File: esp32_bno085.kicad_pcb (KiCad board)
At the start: 2 copper layers, 24.5 x 53.4 mm, 36 parts, among them J1 530480210, J2 USB_C_Receptacle_USB2.0_16P, Q1 AO3401A, SW1 RESET, SW2 BOOT, U1 TP4056-42-ESOP8, U2 ESP32-S3-WROOM-1, U3 BNO085, U4 XC6220B331MR, Y1 32.7680kHz

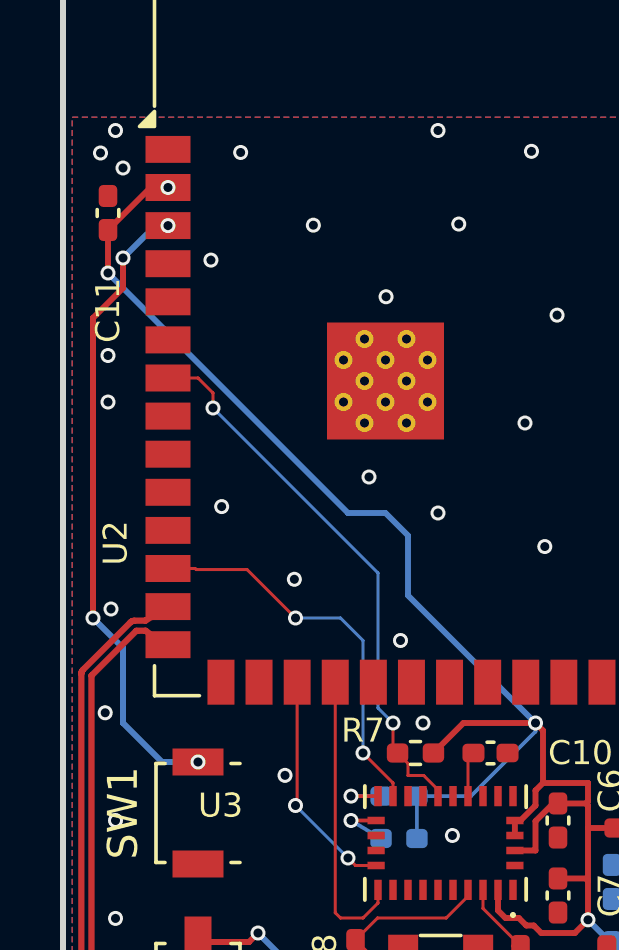
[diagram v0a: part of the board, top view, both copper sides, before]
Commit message: Improve JLCPCB assembly via handling
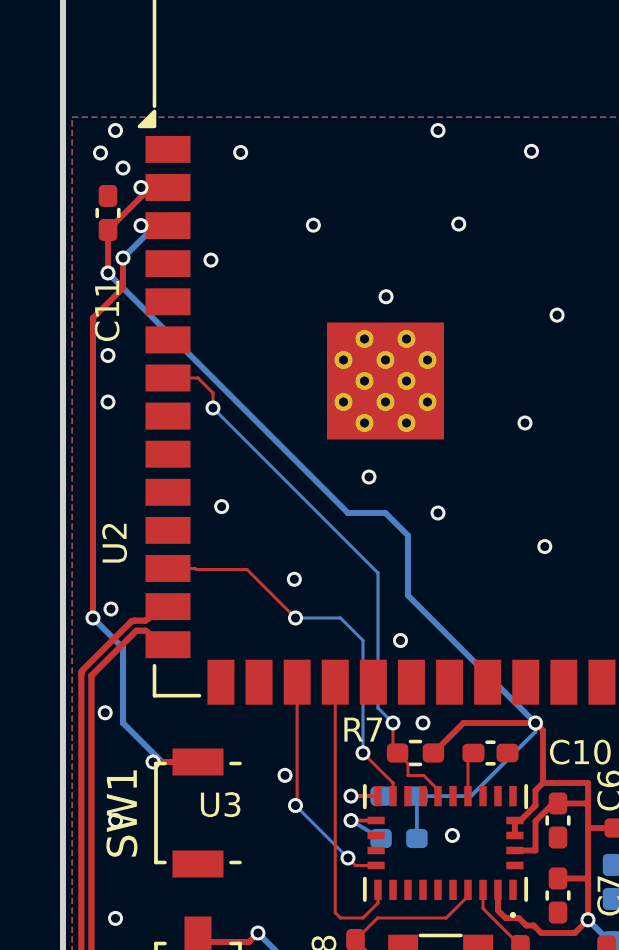
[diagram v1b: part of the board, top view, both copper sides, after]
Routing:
- net ESP_EN: track 21.4 -> 23.3 mm
- net +3.3V: track 59.8 -> 60.4 mm

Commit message: Clarify VSYS rail and JLCPCB order notes
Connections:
- net Net-(D1-K) renamed VSYS
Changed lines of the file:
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@@
 			(layers "F.Cu" "F.Mask" "F.Paste")
 			(roundrect_rratio 0.25)
-			(net "Net-(D1-K)")
+			(net "VSYS")
 			(pinfunction "K")
 			(pintype "passive")
@@
 			(layers "F.Cu" "F.Mask" "F.Paste")
 			(roundrect_rratio 0.25)
-			(net "Net-(D1-K)")
+			(net "VSYS")
 			(pinfunction "D")
 			(pintype "passive")
@@
 			(layers "B.Cu" "B.Mask" "B.Paste")
 			(roundrect_rratio 0.25)
-			(net "Net-(D1-K)")
+			(net "VSYS")
 			(pinfunction "VIN")
 			(pintype "power_in")
@@
 			(layers "B.Cu" "B.Mask" "B.Paste")
 			(roundrect_rratio 0.25)
-			(net "Net-(D1-K)")
+			(net "VSYS")
 			(pinfunction "CE")
 			(pintype "input")
@@
 			(layers "B.Cu" "B.Mask" "B.Paste")
 			(roundrect_rratio 0.25)
-			(net "Net-(D1-K)")
+			(net "VSYS")
 			(pintype "passive")
 		)
@@
 		(width 0.101702)
 		(layer "F.Cu")
-		(net "Net-(D1-K)")
+		(net "VSYS")
 	)
 	(segment
@@
 		(width 0.101702)
 		(layer "F.Cu")
-		(net "Net-(D1-K)")
+		(net "VSYS")
 	)
 	(segment
@@
 		(width 0.101702)
 		(layer "F.Cu")
-		(net "Net-(D1-K)")
+		(net "VSYS")
 	)
 	(segment
@@
 		(width 0.101702)
 		(layer "F.Cu")
-		(net "Net-(D1-K)")
+		(net "VSYS")
 	)
 	(segment
@@
 		(width 0.101702)
 		(layer "F.Cu")
-		(net "Net-(D1-K)")
+		(net "VSYS")
 	)
 	(segment
@@
 		(width 0.101702)
 		(layer "F.Cu")
-		(net "Net-(D1-K)")
+		(net "VSYS")
 	)
 	(segment
@@
 		(width 0.101702)
 		(layer "F.Cu")
-		(net "Net-(D1-K)")
+		(net "VSYS")
 	)
 	(via
@@
 		)
 		(filling no)
-		(net "Net-(D1-K)")
+		(net "VSYS")
 	)
 	(via
@@
 		)
 		(filling no)
-		(net "Net-(D1-K)")
+		(net "VSYS")
 	)
 	(segment
@@
 		(width 0.101702)
 		(layer "B.Cu")
-		(net "Net-(D1-K)")
+		(net "VSYS")
 	)
 	(segment
@@
 		(width 0.101702)
 		(layer "B.Cu")
-		(net "Net-(D1-K)")
+		(net "VSYS")
 	)
 	(segment
@@
 		(width 0.101702)
 		(layer "B.Cu")
-		(net "Net-(D1-K)")
+		(net "VSYS")
 	)
 	(segment
@@
 		(width 0.101702)
 		(layer "B.Cu")
-		(net "Net-(D1-K)")
+		(net "VSYS")
 	)
 	(segment
@@
 		(width 0.101702)
 		(layer "B.Cu")
-		(net "Net-(D1-K)")
+		(net "VSYS")
 	)
 	(segment
@@
 		(width 0.101702)
 		(layer "B.Cu")
-		(net "Net-(D1-K)")
+		(net "VSYS")
 	)
 	(segment
@@
 		(width 0.101702)
 		(layer "B.Cu")
-		(net "Net-(D1-K)")
+		(net "VSYS")
 	)
 	(segment
@@
 		(width 0.101702)
 		(layer "B.Cu")
-		(net "Net-(D1-K)")
+		(net "VSYS")
 	)
 	(segment
@@
 		(width 0.101702)
 		(layer "B.Cu")
-		(net "Net-(D1-K)")
+		(net "VSYS")
 	)
 	(segment
@@
 		(width 0.101702)
 		(layer "B.Cu")
-		(net "Net-(D1-K)")
+		(net "VSYS")
 	)
 	(segment
@@
 		(width 0.101702)
 		(layer "B.Cu")
-		(net "Net-(D1-K)")
+		(net "VSYS")
 	)
 	(segment
@@
 		(width 0.101702)
 		(layer "B.Cu")
-		(net "Net-(D1-K)")
+		(net "VSYS")
 	)
 	(segment
@@
 		(width 0.101702)
 		(layer "B.Cu")
-		(net "Net-(D1-K)")
+		(net "VSYS")
 	)
 	(segment
@@
 		(width 0.101702)
 		(layer "B.Cu")
-		(net "Net-(D1-K)")
+		(net "VSYS")
 	)
 	(segment
@@
 		(width 0.101702)
 		(layer "B.Cu")
-		(net "Net-(D1-K)")
+		(net "VSYS")
 	)
 	(segment
@@
 		(width 0.101702)
 		(layer "B.Cu")
-		(net "Net-(D1-K)")
+		(net "VSYS")
 	)
 	(zone

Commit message: Clarify stock scope and add PCB fiducials
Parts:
- added FID1: Fiducial_1mm_Mask2mm, Fiducial:Fiducial_1mm_Mask2mm, F.Cu at (102.5, 88.0)
- added FID2: Fiducial_1mm_Mask2mm, Fiducial:Fiducial_1mm_Mask2mm, F.Cu at (120.0, 88.0)
- added FID3: Fiducial_1mm_Mask2mm, Fiducial:Fiducial_1mm_Mask2mm, F.Cu at (120.0, 91.0)
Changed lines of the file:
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@@
 			)
 		)
-		(property "BOM Comments" "LCSC page showed this part out of stock on 2026-07-13; verify JLCPCB pre-order/availability before PCBA."
+		(property "BOM Comments" "Lab inventory available per user; stock verification intentionally skipped. If using JLC-sourced turnkey PCBA, re-check C5189642 availability."
 			(at 0 0 180)
 			(unlocked yes)
@@
 		)
 	)
+	(footprint "Fiducial:Fiducial_1mm_Mask2mm"
+		(layer "F.Cu")
+		(at 102.5 88)
+		(descr "Fiducial, circular marking, 1mm bare copper, 2mm soldermask opening")
+		(tags "fiducial")
+		(property "Reference" "FID1"
+			(at 0 -1.95 0)
+			(layer "F.SilkS")
+			(hide yes)
+			(effects
+				(font
+					(size 1 1)
+					(thickness 0.15)
+				)
+			)
+		)
+		(property "Value" "Fiducial_1mm_Mask2mm"
+			(at 0 1.95 0)
+			(layer "F.Fab")
+			(hide yes)
+			(effects
+				(font
+					(size 1 1)
+					(thickness 0.15)
+				)
+			)
+		)
+		(attr smd board_only exclude_from_pos_files exclude_from_bom)
+		(duplicate_pad_numbers_are_jumpers no)
+		(fp_circle
+			(center 0 0)
+			(end 1.25 0)
+			(stroke
+				(width 0.05)
+				(type solid)
+			)
+			(fill no)
+			(layer "F.CrtYd")
+		)
+		(fp_circle
+			(center 0 0)
+			(end 1 0)
+			(stroke
+				(width 0.1)
+				(type solid)
+			)
+			(fill no)
+			(layer "F.Fab")
+		)
+		(pad "" smd circle
+			(at 0 0)
+			(size 1 1)
+			(layers "F.Cu" "F.Mask")
+			(solder_mask_margin 0.5)
+			(clearance 0.6)
+		)
+		(embedded_fonts no)
+	)
+	(footprint "Fiducial:Fiducial_1mm_Mask2mm"
+		(layer "F.Cu")
+		(at 120 88)
+		(descr "Fiducial, circular marking, 1mm bare copper, 2mm soldermask opening")
+		(tags "fiducial")
+		(property "Reference" "FID2"
+			(at 0 -1.95 0)
+			(layer "F.SilkS")
+			(hide yes)
+			(effects
+				(font
+					(size 1 1)
+					(thickness 0.15)
+				)
+			)
+		)
+		(property "Value" "Fiducial_1mm_Mask2mm"
+			(at 0 1.95 0)
+			(layer "F.Fab")
+			(hide yes)
+			(effects
+				(font
+					(size 1 1)
+					(thickness 0.15)
+				)
+			)
+		)
+		(attr smd board_only exclude_from_pos_files exclude_from_bom)
+		(duplicate_pad_numbers_are_jumpers no)
+		(fp_circle
+			(center 0 0)
+			(end 1.25 0)
+			(stroke
+				(width 0.05)
+				(type solid)
+			)
+			(fill no)
+			(layer "F.CrtYd")
+		)
+		(fp_circle
+			(center 0 0)
+			(end 1 0)
+			(stroke
+				(width 0.1)
+				(type solid)
+			)
+			(fill no)
+			(layer "F.Fab")
+		)
+		(pad "" smd circle
+			(at 0 0)
+			(size 1 1)
+			(layers "F.Cu" "F.Mask")
+			(solder_mask_margin 0.5)
+			(clearance 0.6)
+		)
+		(embedded_fonts no)
+	)
+	(footprint "Fiducial:Fiducial_1mm_Mask2mm"
+		(layer "F.Cu")
+		(at 120 91)
+		(descr "Fiducial, circular marking, 1mm bare copper, 2mm soldermask opening")
+		(tags "fiducial")
+		(property "Reference" "FID3"
+			(at 0 -1.95 0)
+			(layer "F.SilkS")
+			(hide yes)
+			(effects
+				(font
+					(size 1 1)
+					(thickness 0.15)
+				)
+			)
+		)
+		(property "Value" "Fiducial_1mm_Mask2mm"
+			(at 0 1.95 0)
+			(layer "F.Fab")
+			(hide yes)
+			(effects
+				(font
+					(size 1 1)
+					(thickness 0.15)
+				)
+			)
+		)
+		(attr smd board_only exclude_from_pos_files exclude_from_bom)
+		(duplicate_pad_numbers_are_jumpers no)
+		(fp_circle
+			(center 0 0)
+			(end 1.25 0)
+			(stroke
+				(width 0.05)
+				(type solid)
+			)
+			(fill no)
+			(layer "F.CrtYd")
+		)
+		(fp_circle
+			(center 0 0)
+			(end 1 0)
+			(stroke
+				(width 0.1)
+				(type solid)
+			)
+			(fill no)
+			(layer "F.Fab")
+		)
+		(pad "" smd circle
+			(at 0 0)
+			(size 1 1)
+			(layers "F.Cu" "F.Mask")
+			(solder_mask_margin 0.5)
+			(clearance 0.6)
+		)
+		(embedded_fonts no)
+	)
 	(gr_rect

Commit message: Normalize capacitor BOM value and refresh JLC notes
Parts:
- C5: value 0.1uf -> 0.1uF
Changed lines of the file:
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@@
 			)
 		)
-		(property "Value" "0.1uf"
+		(property "Value" "0.1uF"
 			(at -0.25 0.75 0)
 			(layer "F.SilkS")

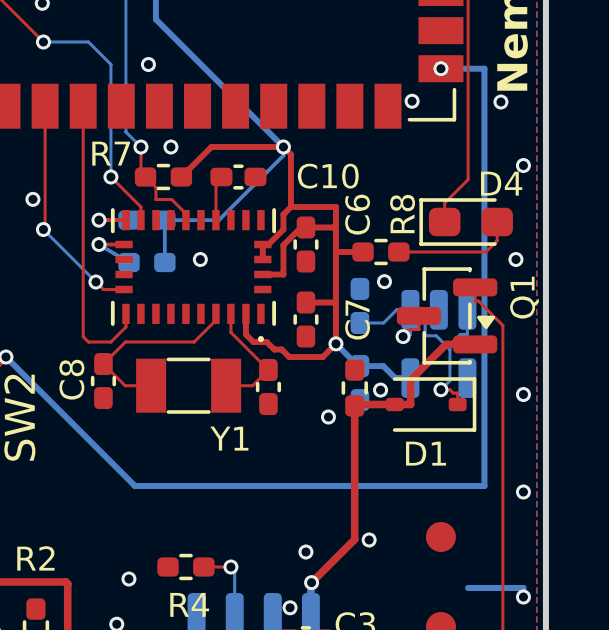
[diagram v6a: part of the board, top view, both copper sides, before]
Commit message: Fix Q1 power path orientation
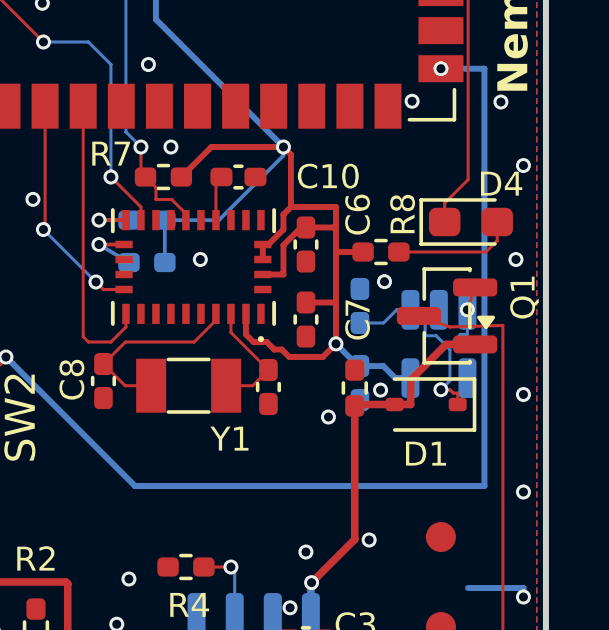
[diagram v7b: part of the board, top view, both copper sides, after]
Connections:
- Q1 pad 2: BAT -> VSYS
- Q1 pad 3: VSYS -> BAT
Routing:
- net VSYS: track 10.5 -> 9.13 mm
- net BAT: track 25.6 -> 26.8 mm
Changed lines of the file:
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@@
 			(layers "F.Cu" "F.Mask" "F.Paste")
 			(roundrect_rratio 0.25)
-			(net "BAT")
+			(net "VSYS")
 			(pinfunction "S")
 			(pintype "passive")
@@
 			(layers "F.Cu" "F.Mask" "F.Paste")
 			(roundrect_rratio 0.25)
-			(net "VSYS")
+			(net "BAT")
 			(pinfunction "D")
 			(pintype "passive")
@@
 	)
 	(segment
-		(start 122.064334 80.949143)
-		(end 121.250785 80.135594)
+		(start 119.2665 80.63)
+		(end 120.3 81)
 		(width 0.101702)
 		(layer "F.Cu")
@@
 	)
 	(segment
-		(start 121.1415 80.135594)
-		(end 121.1415 79.68)
+		(start 120.3 81)
+		(end 122.064334 80.949143)
 		(width 0.101702)
 		(layer "F.Cu")
@@
 	)
 	(segment
-		(start 121.250785 80.135594)
-		(end 121.1415 80.135594)
-		(width 0.101702)
-		(layer "F.Cu")
-		(net "BAT")
-	)
-	(segment
 		(start 114.9325 97.49097)
 		(end 114.9325 98.5483)
@@
 	)
 	(segment
-		(start 118.737833 81.319924)
-		(end 118.972163 81.085594)
+		(start 121.1415 79.68)
+		(end 120.881 80.4275)
 		(width 0.101702)
 		(layer "F.Cu")
@@
 		(net "VSYS")
 	)
-	(segment
-		(start 118.972163 81.085594)
-		(end 119.2665 81.085594)
-		(width 0.101702)
-		(layer "F.Cu")
-		(net "VSYS")
-	)
-	(segment
-		(start 119.2665 81.085594)
-		(end 119.2665 80.63)
-		(width 0.101702)
-		(layer "F.Cu")
-		(net "VSYS")
-	)
 	(via
-		(at 120 83.09051)
+		(at 120.881 80.4275)
 		(size 0.5)
 		(drill 0.3)
@@
 	)
 	(via
-		(at 118.737833 81.319924)
+		(at 120 83.09051)
 		(size 0.5)
 		(drill 0.3)
@@
 	)
 	(segment
-		(start 118.90667 81.319924)
-		(end 118.737833 81.319924)
-		(width 0.101702)
-		(layer "B.Cu")
-		(net "VSYS")
-	)
-	(segment
 		(start 120.298946 81.748541)
 		(end 120.223609 81.673205)
@@
 	)
 	(segment
-		(start 118.981 80.4275)
-		(end 118.981 81.245594)
-		(width 0.101702)
-		(layer "B.Cu")
-		(net "VSYS")
-	)
-	(segment
 		(start 118.087406 80.8655)
 		(end 118.525406 80.4275)
 		(width 0.101702)
 		(layer "B.Cu")
-		(net "VSYS")
-	)
-	(segment
-		(start 118.981 81.245594)
-		(end 118.90667 81.319924)
-		(width 0.101702)
-		(layer "B.Cu")
